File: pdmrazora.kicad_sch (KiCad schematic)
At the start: 9 parts, among them J1 6473418-1, J2 M6_VBAT, J3 M6_GND

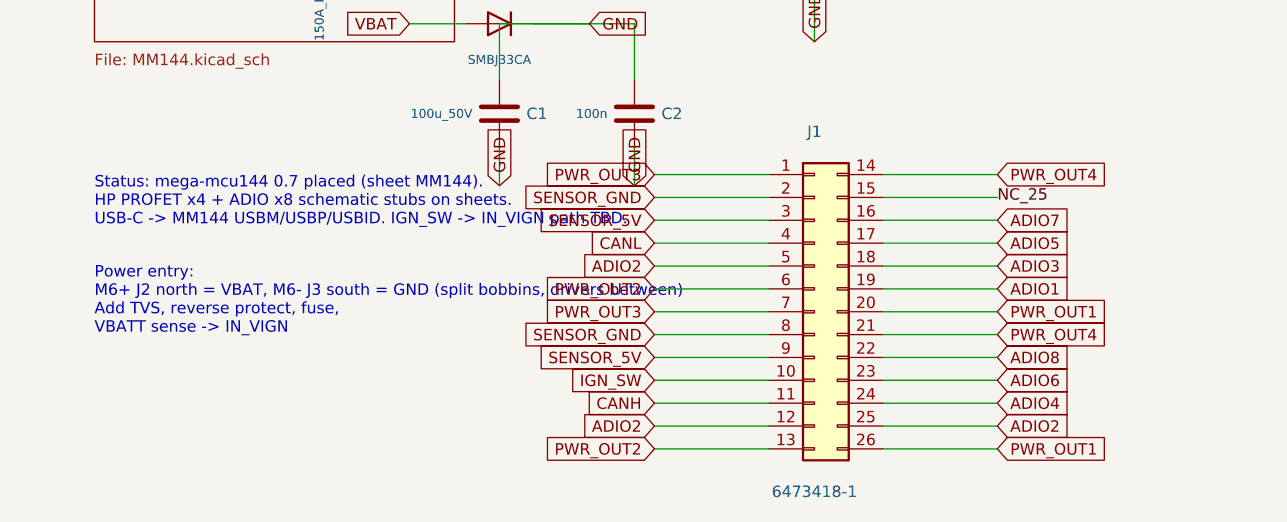
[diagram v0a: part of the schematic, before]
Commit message: Drop even ADIO channels to 4 HP + 4 low-current outputs. (#28)
Remove ADIO2/4/6/8 drivers, sense parts, and pours, leave their SuperSeal pins no-connect, and keep the odd 8 A necks and the HP pours. Rewire J1 so schematic pin numbers match the loom, and stop the odd pull-ups from merging SENSOR_5V into IO2.

Co-authored-by: Cursor Agent <cursoragent@cursor.com>
Co-authored-by: Quintin <quintinbannink42@users.noreply.github.com>
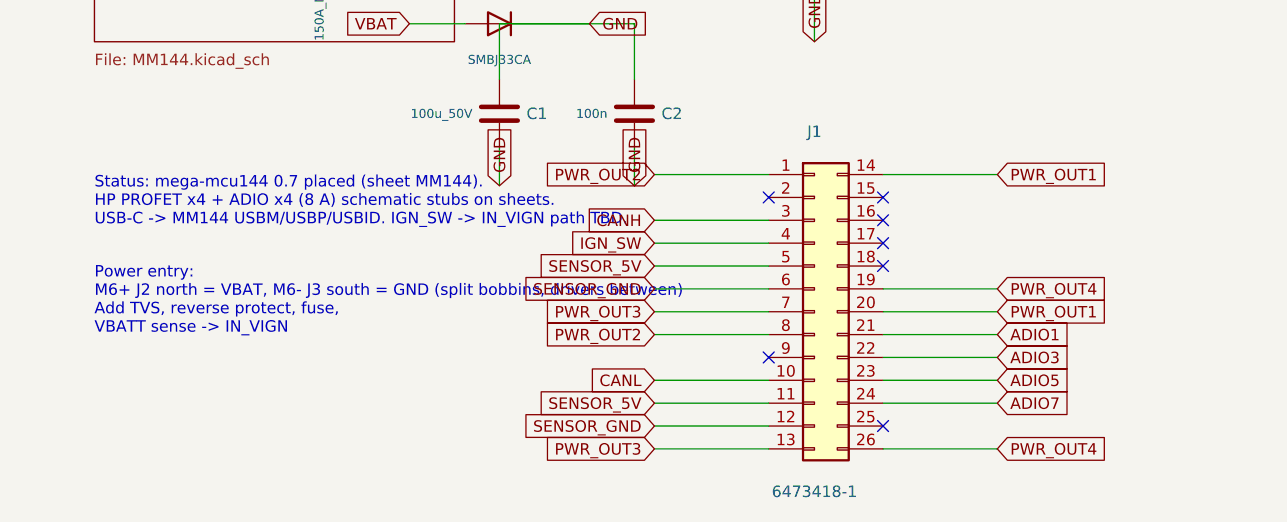
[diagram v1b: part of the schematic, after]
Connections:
- net ADIO4 is gone; now on net ADIO7: J1.24 (Pin_24)
- net ADIO6 is gone; now on net ADIO5: J1.23 (Pin_23)
- net ADIO8 is gone; now on net ADIO3: J1.22 (Pin_22)
- net ADIO1: now also J1.21 (Pin_21); no longer J1.19 (Pin_19)
- net ADIO3: no longer J1.18 (Pin_18)
- net ADIO5: no longer J1.17 (Pin_17)
- net ADIO7: no longer J1.16 (Pin_16)
- net CANH: now also J1.3 (Pin_3); no longer J1.11 (Pin_11)
- net CANL: now also J1.10 (Pin_10); no longer J1.4 (Pin_4)
- net IGN_SW: now also J1.4 (Pin_4); no longer J1.10 (Pin_10)
- net PWR_OUT1: now also J1.14 (Pin_14); no longer J1.26 (Pin_26)
- net PWR_OUT2: now also J1.1 (Pin_1), J1.8 (Pin_8); no longer J1.13 (Pin_13), J1.6 (Pin_6)
- net PWR_OUT3: now also J1.13 (Pin_13); no longer J1.1 (Pin_1)
- net PWR_OUT4: now also J1.19 (Pin_19), J1.26 (Pin_26); no longer J1.14 (Pin_14), J1.21 (Pin_21)
- net SENSOR_5V: now also J1.11 (Pin_11), J1.5 (Pin_5); no longer J1.3 (Pin_3), J1.9 (Pin_9)
- net SENSOR_GND: now also J1.12 (Pin_12), J1.6 (Pin_6); no longer J1.2 (Pin_2), J1.8 (Pin_8)
- removed net ADIO2: J1.12 (Pin_12), J1.25 (Pin_25), J1.5 (Pin_5)
- net NC_25: no longer names the net of J1.15 (Pin_15)
- no-connect marks 0 -> 7
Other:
- note added: "Status: mega-mcu144 0.7 placed (sheet MM144). HP PROFET x4 + ADIO x4 (8 A) schematic stubs on sheets. USB-C -> MM144 USBM/USBP/USBID. IGN_SW -> IN_VIGN path TBD."
- note removed: "Status: mega-mcu144 0.7 placed (sheet MM144). HP PROFET x4 + ADIO x8 schematic stubs on sheets. USB-C -> MM144 USBM/USBP/USBID. IGN_SW -> IN_VIGN path TBD."
